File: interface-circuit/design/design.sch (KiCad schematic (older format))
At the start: 28 parts, among them J1 Raspberry_Pi_2_3, J10 FAN_RELAY, J11 Conn_Switch, J12 Conn_Reset, J2 Screw_Term_RPi, J3 Screw_Term_Detector, J4 12V_IN, J5 Conn_Pwr_LED, J6 Conn_Piezo, J7 Conn_Printer_Mode, J8 Conn_Fan_Mode, J9 PRINTER_RELAY, Q1 2N3904-AP, Q2 2N3904-AP, Q3 2N3904-AP, SW1 SW_SPST, SW2 SW_SPST, U1 LogicLevelConverter_BOB-08745

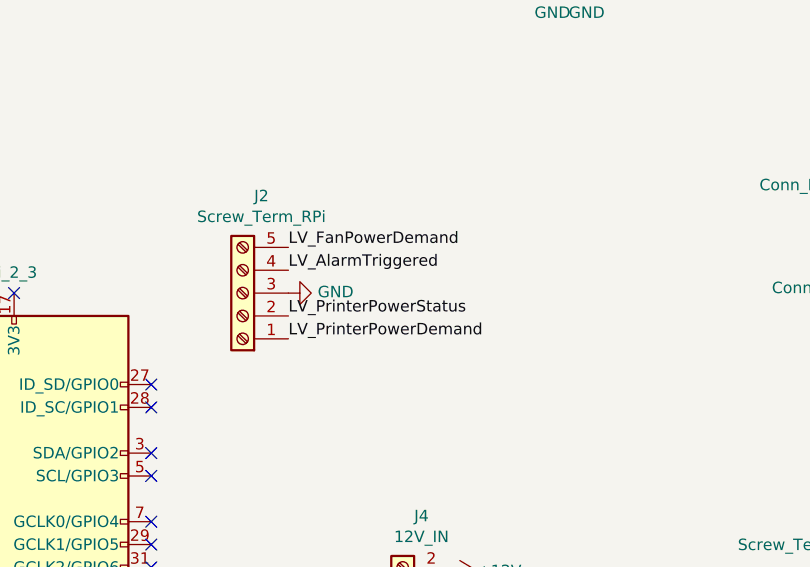
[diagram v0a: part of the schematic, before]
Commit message: Changed protoboard layout so that we are using pins from both sides of the Arduino
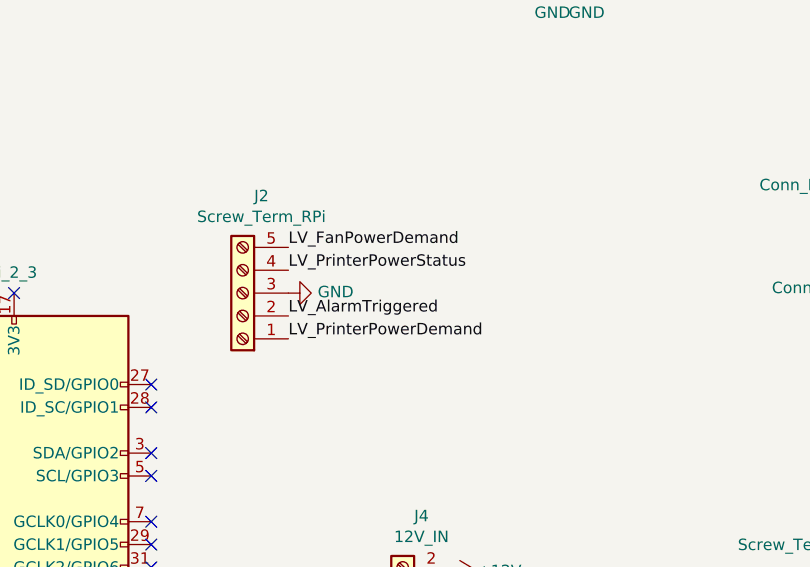
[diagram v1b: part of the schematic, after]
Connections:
- net LV_AlarmTriggered: now also J2.2 (Pin_2); no longer J2.4 (Pin_4)
- net LV_PrinterPowerStatus: now also J2.4 (Pin_4); no longer J2.2 (Pin_2)
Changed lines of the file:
@@
 NoConn ~ 2500 6350
 NoConn ~ 2600 6350
-Text Label 3700 3850 0    50   ~ 0
+Text Label 3700 3650 0    50   ~ 0
 LV_PrinterPowerStatus
 Text Label 3700 3550 0    50   ~ 0
 LV_FanPowerDemand
-Text Label 3700 3650 0    50   ~ 0
+Text Label 3700 3850 0    50   ~ 0
 LV_AlarmTriggered
 $Comp

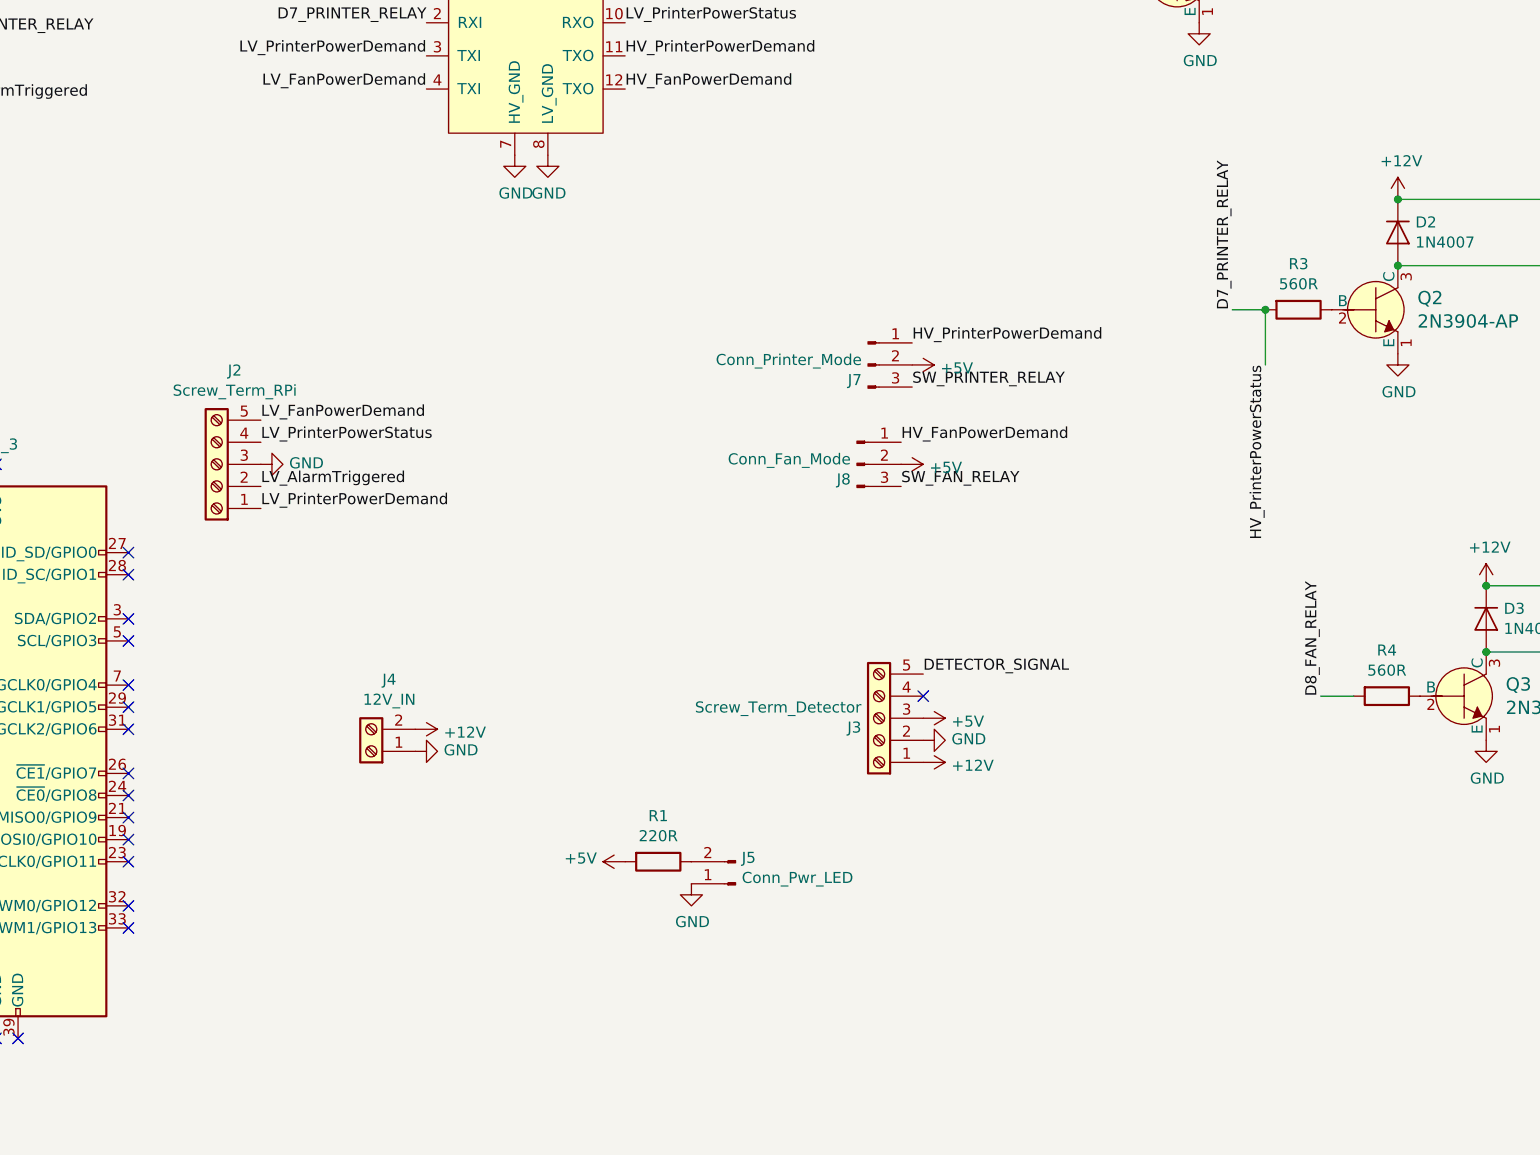
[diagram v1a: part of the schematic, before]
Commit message: Updating eschema with pull down resistors on Arduino inputs
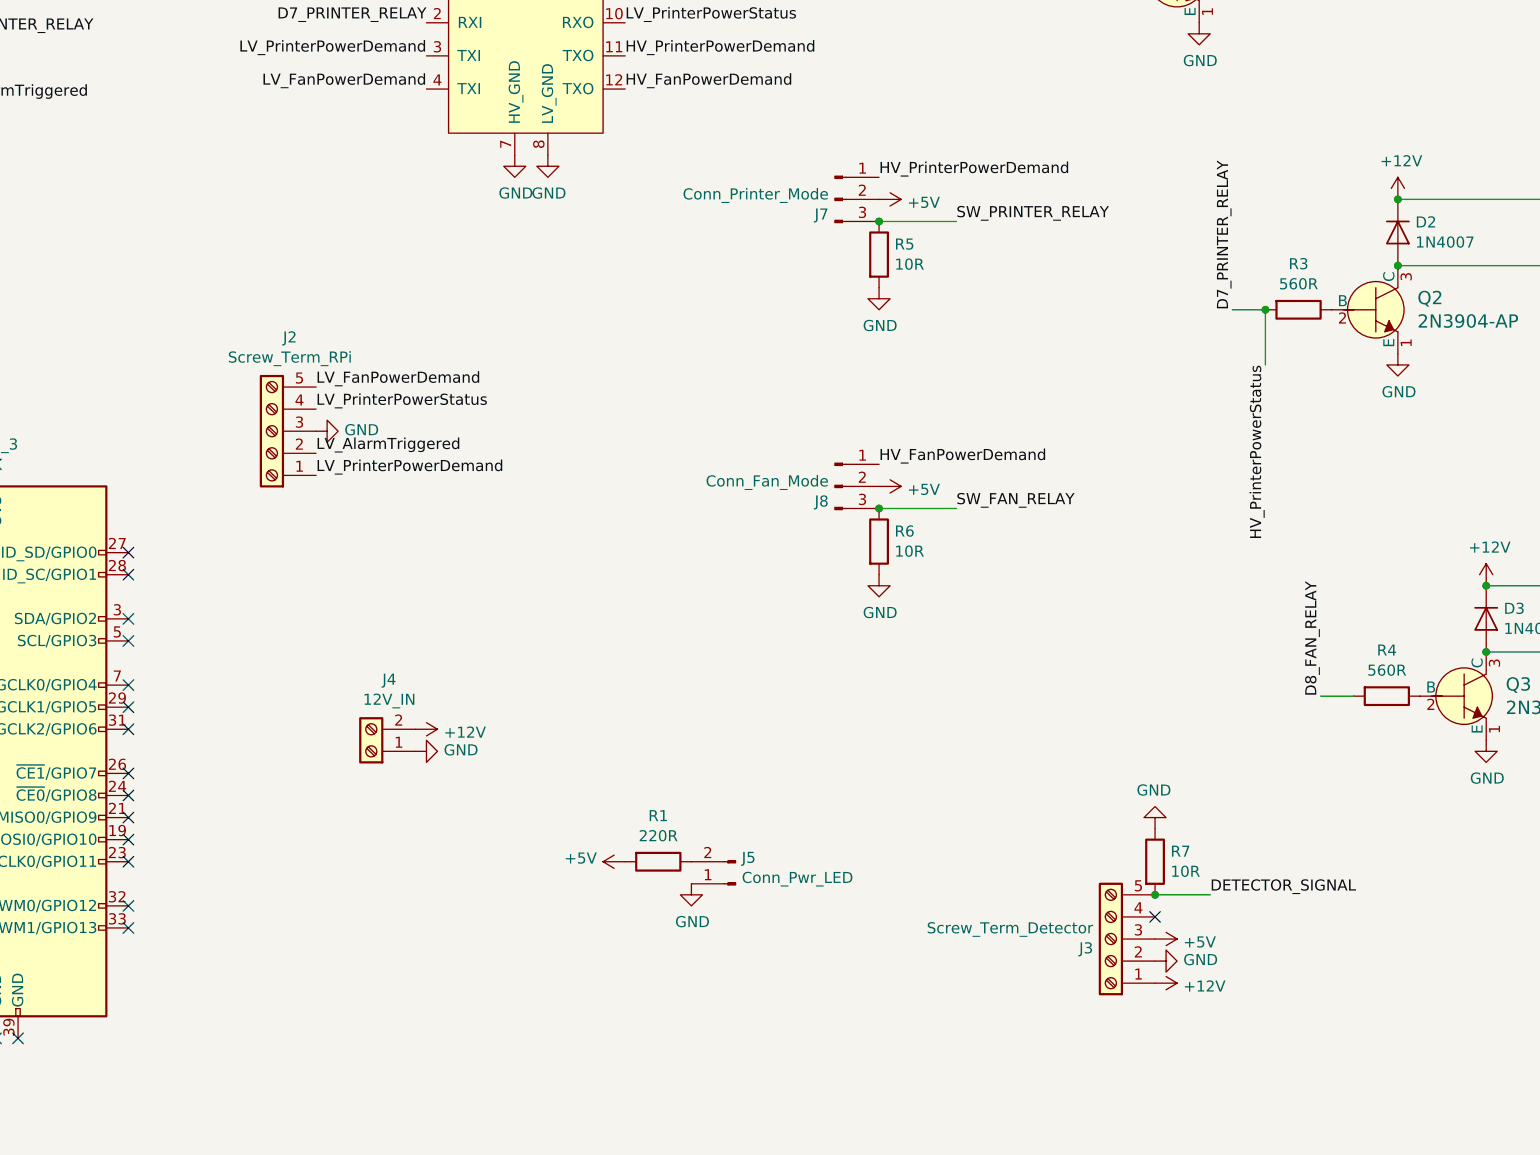
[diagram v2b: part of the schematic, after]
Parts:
- added R5, R6, R7: 10R, symbol Device:R
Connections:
- net DETECTOR_SIGNAL: now also R7.2
- net GND: now also R5.2, R6.2, R7.1
- net SW_FAN_RELAY: now also R6.1
- net SW_PRINTER_RELAY: now also R5.1
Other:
- moved on the sheet: J2, J3, J7, J8
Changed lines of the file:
@@
 NoConn ~ 2500 6350
 NoConn ~ 2600 6350
-Text Label 3700 3650 0    50   ~ 0
+Text Label 3950 3500 0    50   ~ 0
 LV_PrinterPowerStatus
-Text Label 3700 3550 0    50   ~ 0
+Text Label 3950 3400 0    50   ~ 0
 LV_FanPowerDemand
-Text Label 3700 3850 0    50   ~ 0
+Text Label 3950 3700 0    50   ~ 0
 LV_AlarmTriggered
 $Comp
 L power:GND #PWR013
 U 1 1 5CC5D690
-P 3700 3750
-F 0 "#PWR013" H 3700 3500 50  0001 C CNN
-F 1 "GND" V 3705 3622 50  0000 R CNN
-F 2 "" H 3700 3750 50  0001 C CNN
-F 3 "" H 3700 3750 50  0001 C CNN
-	1    3700 3750
+P 3950 3600
+F 0 "#PWR013" H 3950 3350 50  0001 C CNN
+F 1 "GND" V 3955 3472 50  0000 R CNN
+F 2 "" H 3950 3600 50  0001 C CNN
+F 3 "" H 3950 3600 50  0001 C CNN
+	1    3950 3600
 	0    -1   -1   0
 $EndComp
@@
 L Connector:Screw_Terminal_01x05 J3
 U 1 1 5CC995BB
-P 6500 4900
-F 0 "J3" H 6580 4942 50  0000 L CNN
-F 1 "Screw_Term_Detector" H 6580 4851 50  0000 L CNN
-F 2 "digikey-footprints:Term_Block_1x5_P5.08mm" H 6500 4900 50  0001 C CNN
-F 3 "~" H 6500 4900 50  0001 C CNN
-	1    6500 4900
+P 7550 5900
+F 0 "J3" H 7630 5942 50  0000 L CNN
+F 1 "Screw_Term_Detector" H 7630 5851 50  0000 L CNN
+F 2 "digikey-footprints:Term_Block_1x5_P5.08mm" H 7550 5900 50  0001 C CNN
+F 3 "~" H 7550 5900 50  0001 C CNN
+	1    7550 5900
 	-1   0    0    1
 $EndComp
@@
 L power:+12V #PWR016
 U 1 1 5CC9A229
-P 6700 5100
-F 0 "#PWR016" H 6700 4950 50  0001 C CNN
-F 1 "+12V" V 6715 5228 50  0000 L CNN
-F 2 "" H 6700 5100 50  0001 C CNN
-F 3 "" H 6700 5100 50  0001 C CNN
-	1    6700 5100
+P 7750 6100
+F 0 "#PWR016" H 7750 5950 50  0001 C CNN
+F 1 "+12V" V 7765 6228 50  0000 L CNN
+F 2 "" H 7750 6100 50  0001 C CNN
+F 3 "" H 7750 6100 50  0001 C CNN
+	1    7750 6100
 	0    1    1    0
 $EndComp
@@
 L power:GND #PWR015
 U 1 1 5CC9AB9C
-P 6700 5000
-F 0 "#PWR015" H 6700 4750 50  0001 C CNN
-F 1 "GND" V 6705 4872 50  0000 R CNN
-F 2 "" H 6700 5000 50  0001 C CNN
-F 3 "" H 6700 5000 50  0001 C CNN
-	1    6700 5000
+P 7750 6000
+F 0 "#PWR015" H 7750 5750 50  0001 C CNN
+F 1 "GND" V 7755 5872 50  0000 R CNN
+F 2 "" H 7750 6000 50  0001 C CNN
+F 3 "" H 7750 6000 50  0001 C CNN
+	1    7750 6000
 	0    -1   -1   0
 $EndComp
@@
 L power:+5V #PWR014
 U 1 1 5CC9B73F
-P 6700 4900
-F 0 "#PWR014" H 6700 4750 50  0001 C CNN
-F 1 "+5V" V 6715 5028 50  0000 L CNN
-F 2 "" H 6700 4900 50  0001 C CNN
-F 3 "" H 6700 4900 50  0001 C CNN
-	1    6700 4900
+P 7750 5900
+F 0 "#PWR014" H 7750 5750 50  0001 C CNN
+F 1 "+5V" V 7765 6028 50  0000 L CNN
+F 2 "" H 7750 5900 50  0001 C CNN
+F 3 "" H 7750 5900 50  0001 C CNN
+	1    7750 5900
 	0    1    1    0
 $EndComp
 NoConn ~ 5400 300
-NoConn ~ 6700 4800
+NoConn ~ 7750 5800
 $Comp
 L Connector:Screw_Terminal_01x05 J2
 U 1 1 5CCD28E2
-P 3500 3750
-F 0 "J2" H 3418 3325 50  0000 C CNN
-F 1 "Screw_Term_RPi" H 3418 3416 50  0000 C CNN
-F 2 "digikey-footprints:Term_Block_1x5_P5.08mm" H 3500 3750 50  0001 C CNN
-F 3 "~" H 3500 3750 50  0001 C CNN
-	1    3500 3750
+P 3750 3600
+F 0 "J2" H 3668 3175 50  0000 C CNN
+F 1 "Screw_Term_RPi" H 3668 3266 50  0000 C CNN
+F 2 "digikey-footprints:Term_Block_1x5_P5.08mm" H 3750 3600 50  0001 C CNN
+F 3 "~" H 3750 3600 50  0001 C CNN
+	1    3750 3600
 	-1   0    0    1
 $EndComp
-Text Label 3700 3950 0    50   ~ 0
+Text Label 3950 3800 0    50   ~ 0
 LV_PrinterPowerDemand
 NoConn ~ 11500 2050
@@
 L Connector:Conn_01x03_Male J7
 U 1 1 5CCAE331
-P 6450 3300
-F 0 "J7" H 6422 3232 50  0000 R CNN
-F 1 "Conn_Printer_Mode" H 6422 3323 50  0000 R CNN
-F 2 "Connector_PinHeader_2.54mm:PinHeader_1x03_P2.54mm_Vertical" H 6450 3300 50  0001 C CNN
-F 3 "~" H 6450 3300 50  0001 C CNN
-	1    6450 3300
-	1    0    0    -1
-$EndComp
-Text Label 6650 3200 0    50   ~ 0
+P 6300 2550
+F 0 "J7" H 6272 2482 50  0000 R CNN
+F 1 "Conn_Printer_Mode" H 6272 2573 50  0000 R CNN
+F 2 "Connector_PinHeader_2.54mm:PinHeader_1x03_P2.54mm_Vertical" H 6300 2550 50  0001 C CNN
+F 3 "~" H 6300 2550 50  0001 C CNN
+	1    6300 2550
+	1    0    0    -1
+$EndComp
+Text Label 6500 2450 0    50   ~ 0
 HV_PrinterPowerDemand
 Text Label 8100 3050 1    50   ~ 0
 D7_PRINTER_RELAY
-Text Label 6600 3650 0    50   ~ 0
+Text Label 6500 3750 0    50   ~ 0
 HV_FanPowerDemand
 $Comp
@@
 Text Label 1250 1300 2    50   ~ 0
 DETECTOR_SIGNAL
-Text Label 6700 4700 0    50   ~ 0
+Text Label 8000 5700 0    50   ~ 0
 DETECTOR_SIGNAL
 Text Label 1500 5650 2    50   ~ 0
@@
 L Connector:Conn_01x03_Male J8
 U 1 1 5CCBFC14
-P 6400 3750
-F 0 "J8" H 6372 3682 50  0000 R CNN
-F 1 "Conn_Fan_Mode" H 6372 3773 50  0000 R CNN
-F 2 "Connector_PinHeader_2.54mm:PinHeader_1x03_P2.54mm_Vertical" H 6400 3750 50  0001 C CNN
-F 3 "~" H 6400 3750 50  0001 C CNN
-	1    6400 3750
+P 6300 3850
+F 0 "J8" H 6272 3782 50  0000 R CNN
+F 1 "Conn_Fan_Mode" H 6272 3873 50  0000 R CNN
+F 2 "Connector_PinHeader_2.54mm:PinHeader_1x03_P2.54mm_Vertical" H 6300 3850 50  0001 C CNN
+F 3 "~" H 6300 3850 50  0001 C CNN
+	1    6300 3850
 	1    0    0    -1
 $EndComp
@@
 L power:+5V #PWR0102
 U 1 1 5CC5D628
-P 6600 3750
-F 0 "#PWR0102" H 6600 3600 50  0001 C CNN
-F 1 "+5V" V 6615 3878 50  0000 L CNN
-F 2 "" H 6600 3750 50  0001 C CNN
-F 3 "" H 6600 3750 50  0001 C CNN
-	1    6600 3750
+P 6500 3850
+F 0 "#PWR0102" H 6500 3700 50  0001 C CNN
+F 1 "+5V" V 6515 3978 50  0000 L CNN
+F 2 "" H 6500 3850 50  0001 C CNN
+F 3 "" H 6500 3850 50  0001 C CNN
+	1    6500 3850
 	0    1    1    0
 $EndComp
@@
 L power:+5V #PWR0103
 U 1 1 5CC658C6
-P 6650 3300
-F 0 "#PWR0103" H 6650 3150 50  0001 C CNN
-F 1 "+5V" V 6665 3428 50  0000 L CNN
-F 2 "" H 6650 3300 50  0001 C CNN
-F 3 "" H 6650 3300 50  0001 C CNN
-	1    6650 3300
-	0    1    1    0
-$EndComp
-Text Label 6600 3850 0    50   ~ 0
+P 6500 2550
+F 0 "#PWR0103" H 6500 2400 50  0001 C CNN
+F 1 "+5V" V 6515 2678 50  0000 L CNN
+F 2 "" H 6500 2550 50  0001 C CNN
+F 3 "" H 6500 2550 50  0001 C CNN
+	1    6500 2550
+	0    1    1    0
+$EndComp
+Text Label 6850 3950 0    50   ~ 0
 SW_FAN_RELAY
-Text Label 6650 3400 0    50   ~ 0
+Text Label 6850 2650 0    50   ~ 0
 SW_PRINTER_RELAY
 Text Label 2250 1800 0    50   ~ 0
@@
 Text Label 1250 1900 2    50   ~ 0
 D8_FAN_RELAY
+$Comp
+L Device:R R5
+U 1 1 5D10E052
+P 6500 2800
+F 0 "R5" H 6570 2846 50  0000 L CNN
+F 1 "10R" H 6570 2755 50  0000 L CNN
+F 2 "" V 6430 2800 50  0001 C CNN
+F 3 "~" H 6500 2800 50  0001 C CNN
+	1    6500 2800
+	1    0    0    -1
+$EndComp
+$Comp
+L power:GND #PWR0104
+U 1 1 5D10F091
+P 6500 2950
+F 0 "#PWR0104" H 6500 2700 50  0001 C CNN
+F 1 "GND" H 6505 2777 50  0000 C CNN
+F 2 "" H 6500 2950 50  0001 C CNN
+F 3 "" H 6500 2950 50  0001 C CNN
+	1    6500 2950
+	1    0    0    -1
+$EndComp
+$Comp
+L Device:R R6
+U 1 1 5D114FFA
+P 6500 4100
+F 0 "R6" H 6570 4146 50  0000 L CNN
+F 1 "10R" H 6570 4055 50  0000 L CNN
+F 2 "" V 6430 4100 50  0001 C CNN
+F 3 "~" H 6500 4100 50  0001 C CNN
+	1    6500 4100
+	1    0    0    -1
+$EndComp
+$Comp
+L power:GND #PWR0105
+U 1 1 5D115C1F
+P 6500 4250
+F 0 "#PWR0105" H 6500 4000 50  0001 C CNN
+F 1 "GND" H 6505 4077 50  0000 C CNN
+F 2 "" H 6500 4250 50  0001 C CNN
+F 3 "" H 6500 4250 50  0001 C CNN
+	1    6500 4250
+	1    0    0    -1
+$EndComp
+$Comp
+L Device:R R7
+U 1 1 5D12B6A3
+P 7750 5550
+F 0 "R7" H 7820 5596 50  0000 L CNN
+F 1 "10R" H 7820 5505 50  0000 L CNN
+F 2 "" V 7680 5550 50  0001 C CNN
+F 3 "~" H 7750 5550 50  0001 C CNN
+	1    7750 5550
+	1    0    0    -1
+$EndComp
+$Comp
+L power:GND #PWR0106
+U 1 1 5D12C90D
+P 7750 5400
+F 0 "#PWR0106" H 7750 5150 50  0001 C CNN
+F 1 "GND" H 7755 5227 50  0000 C CNN
+F 2 "" H 7750 5400 50  0001 C CNN
+F 3 "" H 7750 5400 50  0001 C CNN
+	1    7750 5400
+	-1   0    0    1
+$EndComp
+Wire Wire Line
+	7750 5700 8000 5700
+Connection ~ 7750 5700
+Wire Wire Line
+	6500 3950 6850 3950
+Connection ~ 6500 3950
+Wire Wire Line
+	6500 2650 6850 2650
+Connection ~ 6500 2650
 $EndSCHEMATC

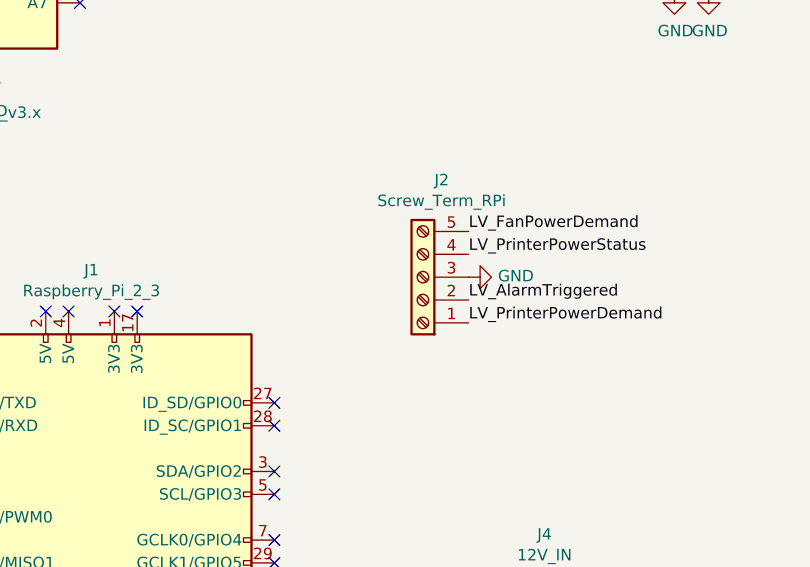
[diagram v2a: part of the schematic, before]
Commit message: adding cable colours to diagram
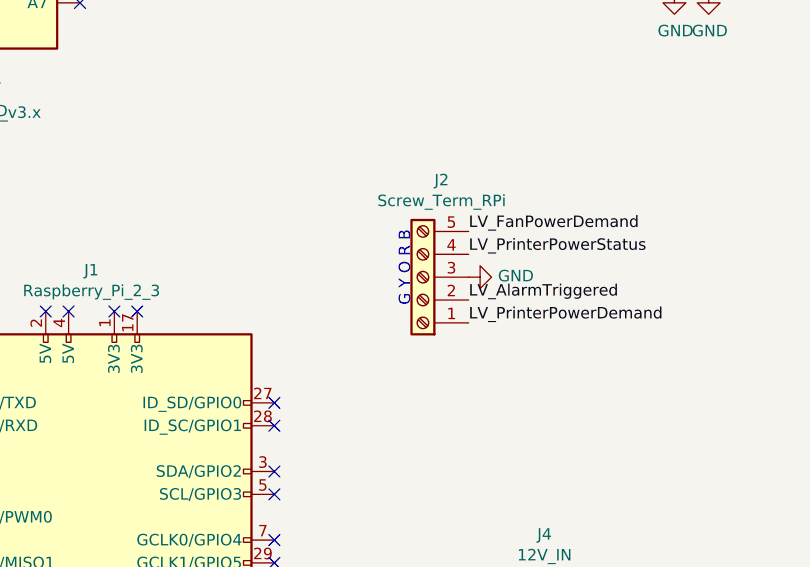
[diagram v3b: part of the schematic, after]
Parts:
- R5, R6, R7: footprint (none) -> Resistor_THT:R_Axial_DIN0207_L6.3mm_D2.5mm_P10.16mm_Horizontal
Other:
- note added: "G Y O R B"
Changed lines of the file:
@@
 F 0 "R5" H 6570 2846 50  0000 L CNN
 F 1 "10R" H 6570 2755 50  0000 L CNN
-F 2 "" V 6430 2800 50  0001 C CNN
+F 2 "Resistor_THT:R_Axial_DIN0207_L6.3mm_D2.5mm_P10.16mm_Horizontal" V 6430 2800 50  0001 C CNN
 F 3 "~" H 6500 2800 50  0001 C CNN
 	1    6500 2800
@@
 F 0 "R6" H 6570 4146 50  0000 L CNN
 F 1 "10R" H 6570 4055 50  0000 L CNN
-F 2 "" V 6430 4100 50  0001 C CNN
+F 2 "Resistor_THT:R_Axial_DIN0207_L6.3mm_D2.5mm_P10.16mm_Horizontal" V 6430 4100 50  0001 C CNN
 F 3 "~" H 6500 4100 50  0001 C CNN
 	1    6500 4100
@@
 F 0 "R7" H 7820 5596 50  0000 L CNN
 F 1 "10R" H 7820 5505 50  0000 L CNN
-F 2 "" V 7680 5550 50  0001 C CNN
+F 2 "Resistor_THT:R_Axial_DIN0207_L6.3mm_D2.5mm_P10.16mm_Horizontal" V 7680 5550 50  0001 C CNN
 F 3 "~" H 7750 5550 50  0001 C CNN
 	1    7750 5550
@@
 	6500 2650 6850 2650
 Connection ~ 6500 2650
+Text Notes 3700 3400 3    50   ~ 0
+G Y O R B
 $EndSCHEMATC
